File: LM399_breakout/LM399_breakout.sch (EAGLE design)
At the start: 15 parts, among them U1 LM399

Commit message: * Final touchups on LM399 breakout board, ready to order!
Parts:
- JP1: value (none) -> VCC
- JP2, JP4: value (none) -> GND
- JP3: value (none) -> Zener
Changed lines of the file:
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@@
 <?xml version="1.0" encoding="utf-8"?>
 <!DOCTYPE eagle SYSTEM "eagle.dtd">
-<eagle version="7.1.0">
+<eagle version="7.2.0">
 <drawing>
 <settings>
@@
 <part name="P+2" library="supply1" deviceset="+15V" device=""/>
 <part name="R2" library="SquantorRCL" deviceset="R-EU_" device="0207/10" value="220k"/>
-<part name="JP1" library="SquantorConnectors" deviceset="PINHD-1X3" device="TH_SMALL"/>
-<part name="JP2" library="SquantorConnectors" deviceset="PINHD-1X3" device="TH_SMALL"/>
-<part name="JP4" library="SquantorConnectors" deviceset="PINHD-1X3" device="TH_SMALL"/>
-<part name="JP3" library="SquantorConnectors" deviceset="PINHD-1X3" device="TH_SMALL"/>
+<part name="JP1" library="SquantorConnectors" deviceset="PINHD-1X3" device="TH_SMALL" value="VCC"/>
+<part name="JP2" library="SquantorConnectors" deviceset="PINHD-1X3" device="TH_SMALL" value="GND"/>
+<part name="JP4" library="SquantorConnectors" deviceset="PINHD-1X3" device="TH_SMALL" value="GND"/>
+<part name="JP3" library="SquantorConnectors" deviceset="PINHD-1X3" device="TH_SMALL" value="Zener"/>
 <part name="GND1" library="supply1" deviceset="GND" device=""/>
 <part name="P+1" library="supply1" deviceset="+15V" device=""/>
@@
 </sheet>
 </sheets>
+<errors>
+</errors>
 </schematic>
 </drawing>

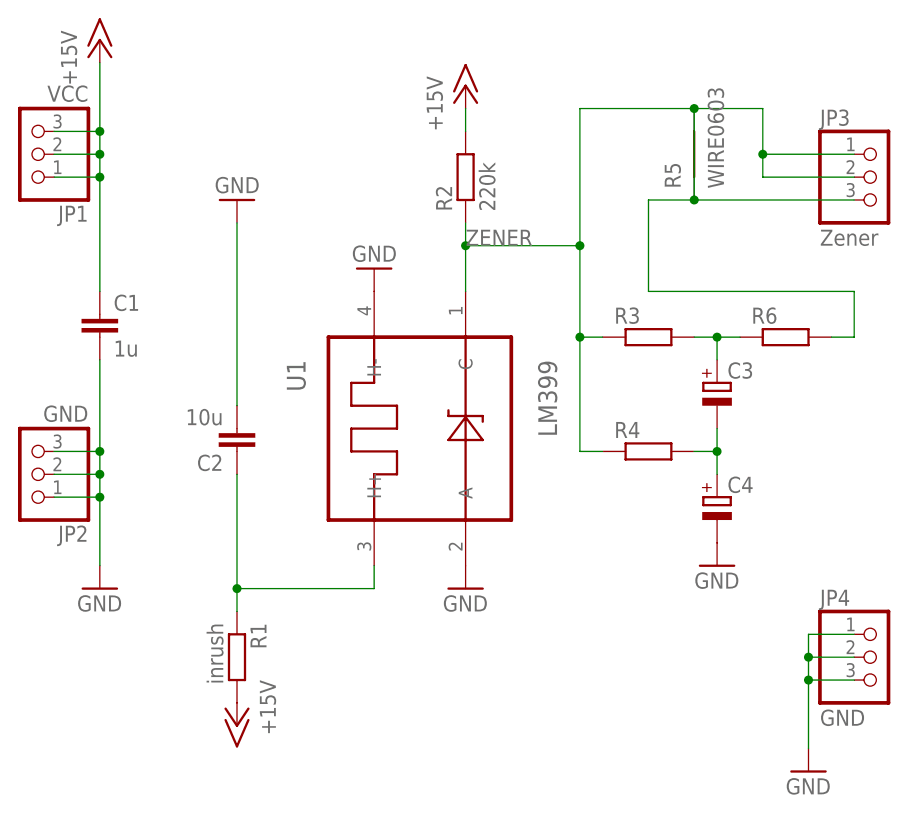
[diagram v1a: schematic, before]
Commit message: * fixed mistakes with the lm399 board
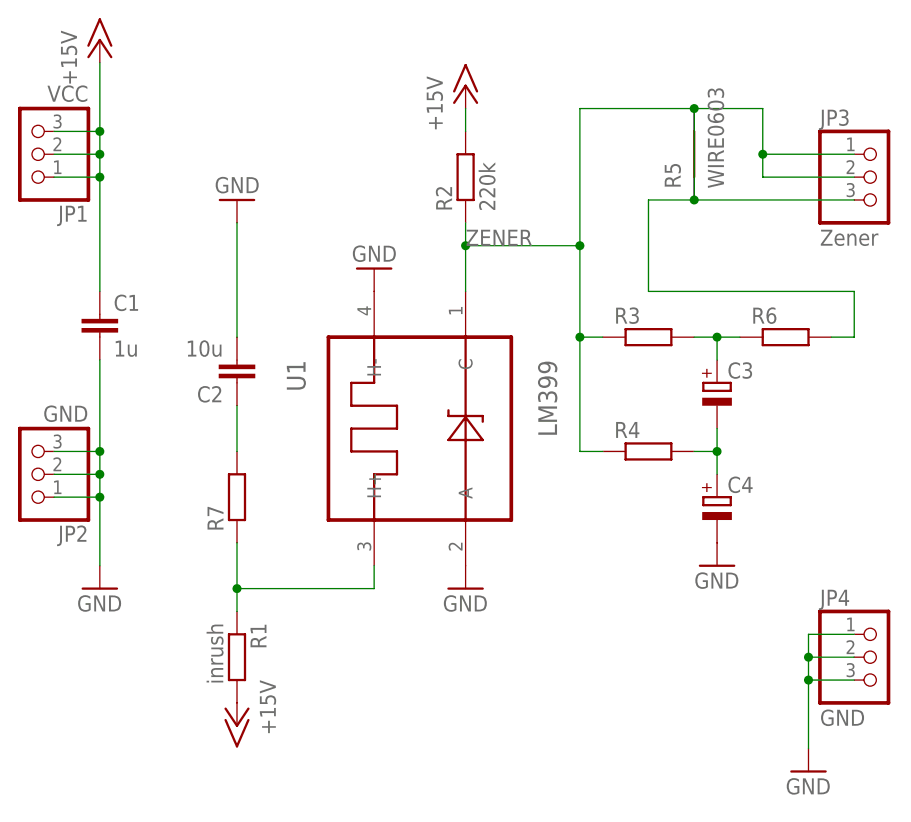
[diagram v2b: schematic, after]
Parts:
- added R7: (no value), SquantorRCL:R-EU_R0603
- C3, C4: device SquantorRCL:CPOL-EUSMCB -> SquantorRCL:CPOL-EUSMCC
- R3, R4, R6: device SquantorRCL:R-EU_0204/7 -> SquantorRCL:R-EU_0207/10
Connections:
- new net N$2: C2.1, R7.2
- net N$1: now also R7.1; no longer C2.1
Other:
- moved on the sheet: C2
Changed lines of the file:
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@@
 <grid distance="0.1" unitdist="inch" unit="inch" style="lines" multiple="1" display="no" altdistance="0.01" altunitdist="inch" altunit="inch"/>
 <layers>
-<layer number="1" name="Top" color="4" fill="1" visible="no" active="no"/>
-<layer number="16" name="Bottom" color="1" fill="1" visible="no" active="no"/>
-<layer number="17" name="Pads" color="2" fill="1" visible="no" active="no"/>
-<layer number="18" name="Vias" color="2" fill="1" visible="no" active="no"/>
-<layer number="19" name="Unrouted" color="6" fill="1" visible="no" active="no"/>
-<layer number="20" name="Dimension" color="15" fill="1" visible="no" active="no"/>
-<layer number="21" name="tPlace" color="7" fill="1" visible="no" active="no"/>
-<layer number="22" name="bPlace" color="7" fill="1" visible="no" active="no"/>
-<layer number="23" name="tOrigins" color="15" fill="1" visible="no" active="no"/>
-<layer number="24" name="bOrigins" color="15" fill="1" visible="no" active="no"/>
-<layer number="25" name="tNames" color="7" fill="1" visible="no" active="no"/>
-<layer number="26" name="bNames" color="7" fill="1" visible="no" active="no"/>
-<layer number="27" name="tValues" color="7" fill="1" visible="no" active="no"/>
-<layer number="28" name="bValues" color="7" fill="1" visible="no" active="no"/>
+<layer number="1" name="Top" color="4" fill="1" visible="yes" active="no"/>
+<layer number="16" name="Bottom" color="1" fill="1" visible="yes" active="no"/>
+<layer number="17" name="Pads" color="2" fill="1" visible="yes" active="no"/>
+<layer number="18" name="Vias" color="2" fill="1" visible="yes" active="no"/>
+<layer number="19" name="Unrouted" color="6" fill="1" visible="yes" active="no"/>
+<layer number="20" name="Dimension" color="15" fill="1" visible="yes" active="no"/>
+<layer number="21" name="tPlace" color="7" fill="1" visible="yes" active="no"/>
+<layer number="22" name="bPlace" color="7" fill="1" visible="yes" active="no"/>
+<layer number="23" name="tOrigins" color="15" fill="1" visible="yes" active="no"/>
+<layer number="24" name="bOrigins" color="15" fill="1" visible="yes" active="no"/>
+<layer number="25" name="tNames" color="7" fill="1" visible="yes" active="no"/>
+<layer number="26" name="bNames" color="7" fill="1" visible="yes" active="no"/>
+<layer number="27" name="tValues" color="7" fill="1" visible="yes" active="no"/>
+<layer number="28" name="bValues" color="7" fill="1" visible="yes" active="no"/>
 <layer number="29" name="tStop" color="7" fill="3" visible="no" active="no"/>
 <layer number="30" name="bStop" color="7" fill="6" visible="no" active="no"/>
@@
 <layer number="35" name="tGlue" color="7" fill="4" visible="no" active="no"/>
 <layer number="36" name="bGlue" color="7" fill="5" visible="no" active="no"/>
-<layer number="37" name="tTest" color="7" fill="1" visible="no" active="no"/>
-<layer number="38" name="bTest" color="7" fill="1" visible="no" active="no"/>
+<layer number="37" name="tTest" color="7" fill="1" visible="yes" active="no"/>
+<layer number="38" name="bTest" color="7" fill="1" visible="yes" active="no"/>
 <layer number="39" name="tKeepout" color="4" fill="11" visible="no" active="no"/>
 <layer number="40" name="bKeepout" color="1" fill="11" visible="no" active="no"/>
@@
 <layer number="44" name="Drills" color="7" fill="1" visible="no" active="no"/>
 <layer number="45" name="Holes" color="7" fill="1" visible="no" active="no"/>
-<layer number="46" name="Milling" color="3" fill="1" visible="no" active="no"/>
-<layer number="47" name="Measures" color="7" fill="1" visible="no" active="no"/>
-<layer number="48" name="Document" color="7" fill="1" visible="no" active="no"/>
-<layer number="49" name="Reference" color="7" fill="1" visible="no" active="no"/>
-<layer number="50" name="dxf" color="7" fill="1" visible="no" active="no"/>
-<layer number="51" name="tDocu" color="7" fill="1" visible="no" active="no"/>
-<layer number="52" name="bDocu" color="7" fill="1" visible="no" active="no"/>
-<layer number="53" name="tGND_GNDA" color="7" fill="9" visible="no" active="no"/>
-<layer number="54" name="bGND_GNDA" color="1" fill="9" visible="no" active="no"/>
-<layer number="56" name="wert" color="7" fill="1" visible="no" active="no"/>
+<layer number="46" name="Milling" color="3" fill="1" visible="yes" active="no"/>
+<layer number="47" name="Measures" color="7" fill="1" visible="yes" active="no"/>
+<layer number="48" name="Document" color="7" fill="1" visible="yes" active="no"/>
+<layer number="49" name="Reference" color="7" fill="1" visible="yes" active="no"/>
+<layer number="50" name="dxf" color="7" fill="1" visible="yes" active="no"/>
+<layer number="51" name="tDocu" color="7" fill="1" visible="yes" active="no"/>
+<layer number="52" name="bDocu" color="7" fill="1" visible="yes" active="no"/>
+<layer number="53" name="tGND_GNDA" color="7" fill="9" visible="yes" active="no"/>
+<layer number="54" name="bGND_GNDA" color="1" fill="9" visible="yes" active="no"/>
+<layer number="56" name="wert" color="7" fill="1" visible="yes" active="no"/>
 <layer number="90" name="Modules" color="5" fill="1" visible="yes" active="yes"/>
 <layer number="91" name="Nets" color="2" fill="1" visible="yes" active="yes"/>
@@
 <part name="GND6" library="supply1" deviceset="GND" device=""/>
 <part name="P+3" library="supply1" deviceset="+15V" device=""/>
-<part name="R3" library="SquantorRCL" deviceset="R-EU_" device="0204/7"/>
-<part name="R4" library="SquantorRCL" deviceset="R-EU_" device="0204/7"/>
-<part name="C3" library="SquantorRCL" deviceset="CPOL-EU" device="SMCB"/>
-<part name="C4" library="SquantorRCL" deviceset="CPOL-EU" device="SMCB"/>
+<part name="R3" library="SquantorRCL" deviceset="R-EU_" device="0207/10"/>
+<part name="R4" library="SquantorRCL" deviceset="R-EU_" device="0207/10"/>
+<part name="C3" library="SquantorRCL" deviceset="CPOL-EU" device="SMCC"/>
+<part name="C4" library="SquantorRCL" deviceset="CPOL-EU" device="SMCC"/>
 <part name="GND5" library="supply1" deviceset="GND" device=""/>
-<part name="R6" library="SquantorRCL" deviceset="R-EU_" device="0204/7"/>
+<part name="R6" library="SquantorRCL" deviceset="R-EU_" device="0207/10"/>
 <part name="R5" library="SquantorRCL" deviceset="WIRE" device="0603"/>
+<part name="R7" library="SquantorRCL" deviceset="R-EU_" device="R0603"/>
 </parts>
 <sheets>
@@
 <instance part="GND3" gate="1" x="58.42" y="60.96" rot="R180"/>
 <instance part="GND4" gate="1" x="68.58" y="25.4"/>
-<instance part="C2" gate="G$1" x="43.18" y="40.64" rot="R180"/>
+<instance part="C2" gate="G$1" x="43.18" y="48.26" rot="R180"/>
 <instance part="GND2" gate="1" x="43.18" y="68.58" rot="R180"/>
 <instance part="R1" gate="G$1" x="43.18" y="17.78" rot="R270"/>
@@
 <instance part="R6" gate="G$1" x="104.14" y="53.34"/>
 <instance part="R5" gate="G$1" x="93.98" y="73.66" rot="R90"/>
+<instance part="R7" gate="G$1" x="43.18" y="35.56" rot="R90"/>
 </instances>
 <busses>
@@
 <pinref part="C2" gate="G$1" pin="2"/>
 <pinref part="GND2" gate="1" pin="GND"/>
-<wire x1="43.18" y1="66.04" x2="43.18" y2="45.72" width="0.1524" layer="91"/>
+<wire x1="43.18" y1="66.04" x2="43.18" y2="53.34" width="0.1524" layer="91"/>
 </segment>
 <segment>
@@
 <segment>
 <pinref part="U1" gate="G$1" pin="H+"/>
-<pinref part="C2" gate="G$1" pin="1"/>
 <wire x1="58.42" y1="25.4" x2="58.42" y2="27.94" width="0.1524" layer="91"/>
-<wire x1="43.18" y1="38.1" x2="43.18" y2="25.4" width="0.1524" layer="91"/>
 <pinref part="R1" gate="G$1" pin="1"/>
 <wire x1="43.18" y1="25.4" x2="43.18" y2="22.86" width="0.1524" layer="91"/>
 <wire x1="58.42" y1="25.4" x2="43.18" y2="25.4" width="0.1524" layer="91"/>
+<pinref part="R7" gate="G$1" pin="1"/>
+<wire x1="43.18" y1="25.4" x2="43.18" y2="30.48" width="0.1524" layer="91"/>
 <junction x="43.18" y="25.4"/>
 </segment>
@@
 <wire x1="111.76" y1="73.66" x2="101.6" y2="73.66" width="0.1524" layer="91"/>
 <junction x="101.6" y="73.66"/>
+<pinref part="R5" gate="G$1" pin="2"/>
+<junction x="93.98" y="78.74"/>
+<pinref part="R5" gate="G$1" pin="1"/>
+<junction x="93.98" y="68.58"/>
 <pinref part="JP3" gate="A" pin="3"/>
+<wire x1="111.76" y1="68.58" x2="93.98" y2="68.58" width="0.1524" layer="91"/>
+<wire x1="88.9" y1="68.58" x2="93.98" y2="68.58" width="0.1524" layer="91"/>
 <pinref part="R6" gate="G$1" pin="2"/>
 <wire x1="109.22" y1="53.34" x2="111.76" y2="53.34" width="0.1524" layer="91"/>
@@
 <wire x1="111.76" y1="58.42" x2="88.9" y2="58.42" width="0.1524" layer="91"/>
 <wire x1="88.9" y1="58.42" x2="88.9" y2="68.58" width="0.1524" layer="91"/>
-<wire x1="88.9" y1="68.58" x2="93.98" y2="68.58" width="0.1524" layer="91"/>
-<pinref part="R5" gate="G$1" pin="1"/>
-<junction x="93.98" y="68.58"/>
-<wire x1="111.76" y1="68.58" x2="93.98" y2="68.58" width="0.1524" layer="91"/>
-<wire x1="93.98" y1="78.74" x2="93.98" y2="68.58" width="0.1524" layer="91"/>
-<pinref part="R5" gate="G$1" pin="2"/>
-<junction x="93.98" y="78.74"/>
+<wire x1="93.98" y1="68.58" x2="93.98" y2="78.74" width="0.1524" layer="91"/>
 </segment>
 </net>
@@
 </segment>
 </net>
+<net name="N$2" class="0">
+<segment>
+<pinref part="R7" gate="G$1" pin="2"/>
+<pinref part="C2" gate="G$1" pin="1"/>
+<wire x1="43.18" y1="40.64" x2="43.18" y2="45.72" width="0.1524" layer="91"/>
+</segment>
+</net>
